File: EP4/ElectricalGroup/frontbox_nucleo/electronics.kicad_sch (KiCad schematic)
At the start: 39 parts, among them J10 CAN_Rpi, J11 fan1, J12 fan2, J13 buzzer, J14 CAN, J15 APPS_BSE, J2 steering, J4 5V, J5 VCC_3V3, J6 sensor_R, J7 sensor_L, J8 24V, J9 Rpi, P1 24Vpower, Q1 PN2222A, U2 LMV358, U3 TCAN332G, U4 TEN_40-2411WIE

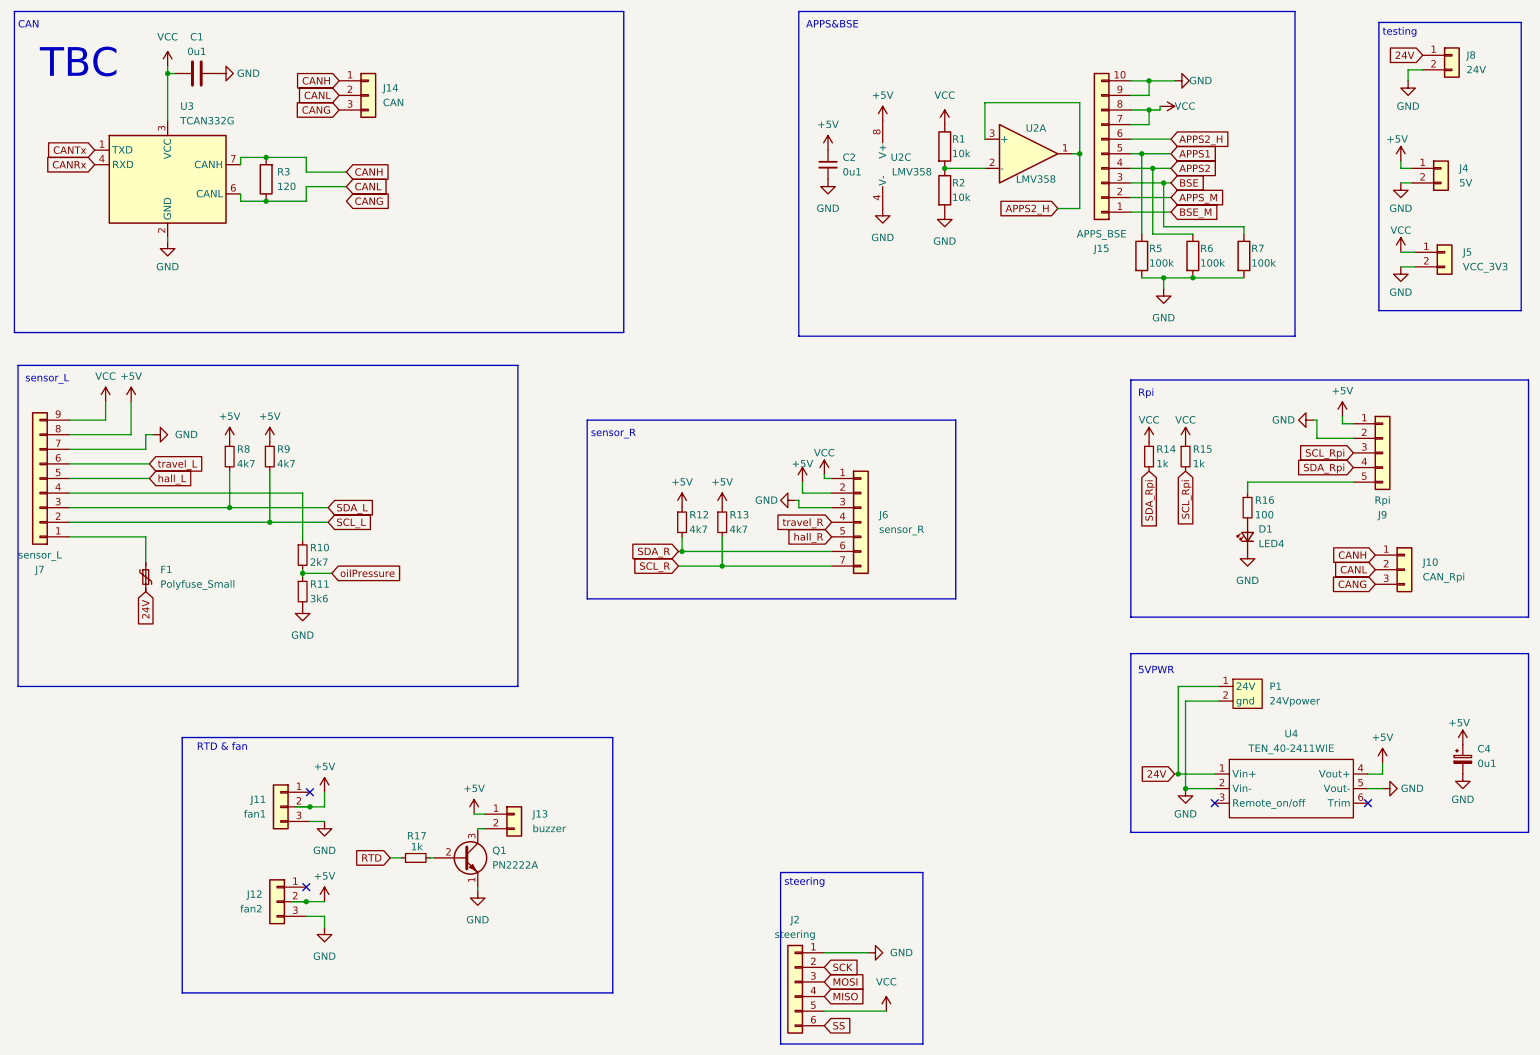
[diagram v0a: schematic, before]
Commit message: use online library for frontbox
replaced: TEN_40-2411WIE, CTM1051AM
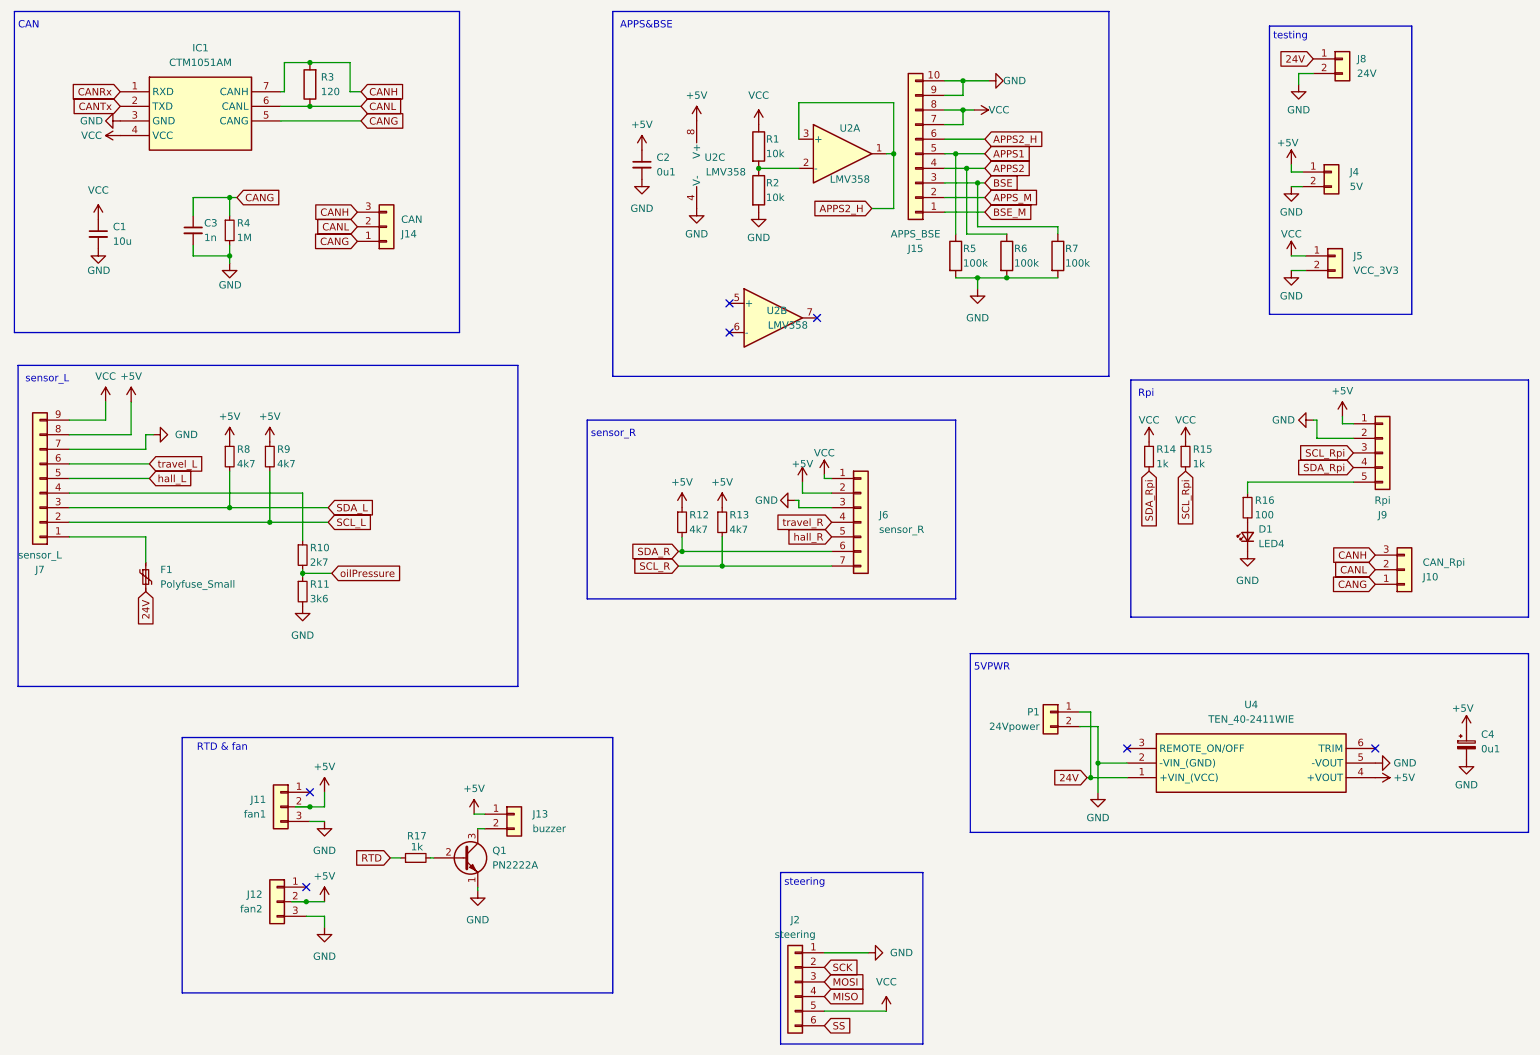
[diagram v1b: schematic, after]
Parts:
- removed C1: 0u1, Capacitor_SMD:C_0603_1608Metric, symbol Device:C
- removed U3: TCAN332G, Package_SO:SOIC-8_3.9x4.9mm_P1.27mm, symbol Interface_CAN_LIN:TCAN332G
- added C1: 10u, Capacitor_SMD:C_0805_2012Metric_Pad1.18x1.45mm_HandSolder, symbol Device:C_Small
- added C3: 1n, Capacitor_THT:C_Disc_D5.0mm_W2.5mm_P5.00mm, symbol Device:C_Small
- added IC1: CTM1051AM, SamacSys_Parts:CTM1051AM, symbol SamacSys_Parts:CTM1051AM
- added R4: 1M, Resistor_SMD:R_0603_1608Metric, symbol Device:R_Small
- added unit 2 of U2
- P1: symbol nturt_kicad_lib:24Vpower -> Connector_Generic:Conn_01x02
- U4: footprint nturt_kicad_lib:TEN 40-2411WIE -> SamacSys_Parts:TEN402411WIE; symbol nturt_kicad_lib:TEN_40-2411WIE -> SamacSys_Parts:TEN_40-2411WIE; Height (none) -> 10.7; Manufacturer_Name (none) -> Traco Power; Manufacturer_Part_Number (none) -> TEN 40-2411WIE; Mouser Part Number (none) -> 495-TEN40-2411WIE; Mouser Price/Stock (none) -> https://www.mouser.co.uk/ProductDetail/TRACO-Power/TEN-40-2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
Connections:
- net CANG: now also J10.1 (Pin_1), J14.1 (Pin_1), C3.1, IC1.5 (CANG), R4.1; no longer J10.3 (Pin_3), J14.3 (Pin_3)
- net CANH: now also J10.3 (Pin_3), J14.3 (Pin_3), IC1.7 (CANH); no longer J10.1 (Pin_1), J14.1 (Pin_1)
- net CANL: now also IC1.6 (CANL)
- net CANRx: now also IC1.1 (RXD)
- net CANTx: now also IC1.2 (TXD)
- net GND: now also C1.2, C3.2, IC1.3 (GND), R4.2
- net VCC: now also C1.1, IC1.4 (VCC)
- no-connect marks 4 -> 7
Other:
- note removed: "TBC"
- moved on the sheet: C2, C4, J14, J15, J4, J5, J8, P1, R1, R2, R3, R5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

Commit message: apply net class on frontbox
power class with 5 mm track width for +5V and VCC
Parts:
- C4: footprint Capacitor_SMD:C_0603_1608Metric -> Capacitor_Tantalum_SMD:CP_EIA-3528-21_Kemet-B_Pad1.50x2.35mm_HandSolder
- U4: footprint SamacSys_Parts:TEN402411WIE -> TEN402411WIE
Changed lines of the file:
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@@
       (effects (font (size 1.27 1.27)) (justify left))
     )
-    (property "Footprint" "Capacitor_SMD:C_0603_1608Metric" (at 269.24 144.78 0)
+    (property "Footprint" "Capacitor_Tantalum_SMD:CP_EIA-3528-21_Kemet-B_Pad1.50x2.35mm_HandSolder" (at 269.24 144.78 0)
       (effects (font (size 1.27 1.27)) hide)
     )
@@
       (effects (font (size 1.27 1.27)))
     )
-    (property "Footprint" "SamacSys_Parts:TEN402411WIE" (at 249.555 240.335 0)
+    (property "Footprint" "TEN402411WIE" (at 249.555 240.335 0)
       (effects (font (size 1.27 1.27)) (justify left top) hide)
     )

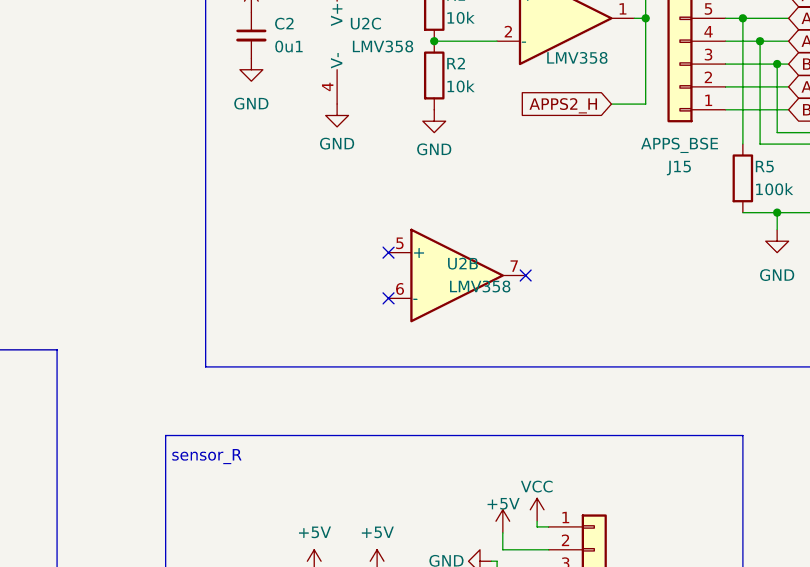
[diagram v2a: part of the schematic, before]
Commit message: frontbox unused opamp update
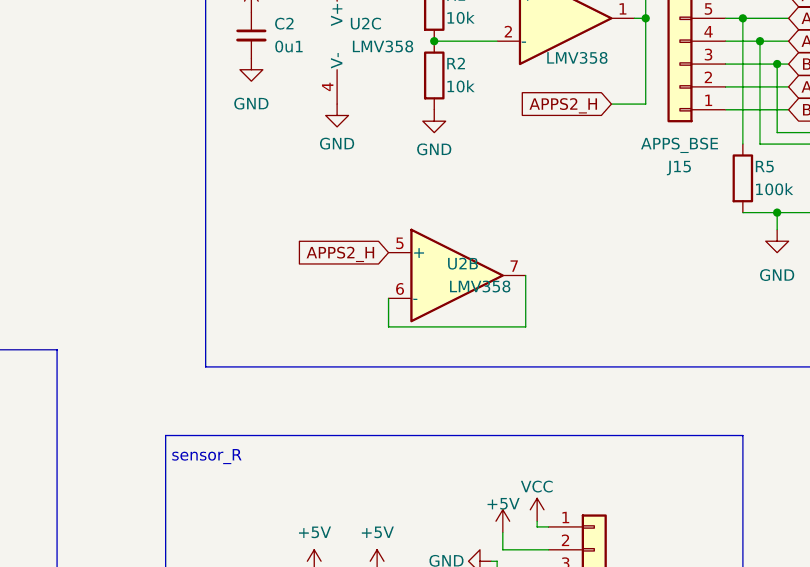
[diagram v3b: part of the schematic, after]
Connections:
- net APPS2_H: now also U2.5 (+)
- net at U2.6 (-): now also U2.7
- no-connect marks 7 -> 4
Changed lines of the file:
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@@
   (junction (at 132.715 111.125) (diameter 0) (color 0 0 0 0)
   )
-  (no_connect (at 140.97 73.025))
   (no_connect (at 67.31 169.545))
   (no_connect (at 67.945 153.035))
   (no_connect (at 253.365 145.415))
-  (no_connect (at 140.97 67.945))
-  (no_connect (at 156.21 70.485))
   (no_connect (at 210.185 145.415))
   (wire (pts (xy 39.37 93.345) (xy 26.035 93.345))
@@
     (stroke (width 0) (type default))
   )
+  (wire (pts (xy 156.21 70.485) (xy 156.21 76.2))
+    (stroke (width 0) (type default))
+  )
   (wire (pts (xy 47.625 57.785) (xy 47.625 59.69))
     (stroke (width 0) (type default))
@@
     (stroke (width 0) (type default))
   )
+  (wire (pts (xy 156.21 76.2) (xy 140.97 76.2))
+    (stroke (width 0) (type default))
+  )
   (wire (pts (xy 168.275 191.135) (xy 157.48 191.135))
     (stroke (width 0) (type default))
@@
     (stroke (width 0) (type default))
   )
+  (wire (pts (xy 140.97 76.2) (xy 140.97 73.025))
+    (stroke (width 0) (type default))
+  )
   (wire (pts (xy 62.865 33.655) (xy 67.945 33.655))
     (stroke (width 0) (type default))
@@
     )
   )
+  (global_label "APPS2_H" (shape input) (at 140.97 67.945 180) (fields_autoplaced)
+    (effects (font (size 1.27 1.27)) (justify right))
+    (property "Intersheetrefs" "${INTERSHEET_REFS}" (at 129.6391 67.945 0)
+      (effects (font (size 1.27 1.27)) (justify right) hide)
+    )
+  )
